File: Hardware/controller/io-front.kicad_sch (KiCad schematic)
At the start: 14 parts, among them J401 Conn_02x10_Odd_Even, J402 Conn_02x05_Odd_Even, J403 Conn_02x08_Odd_Even

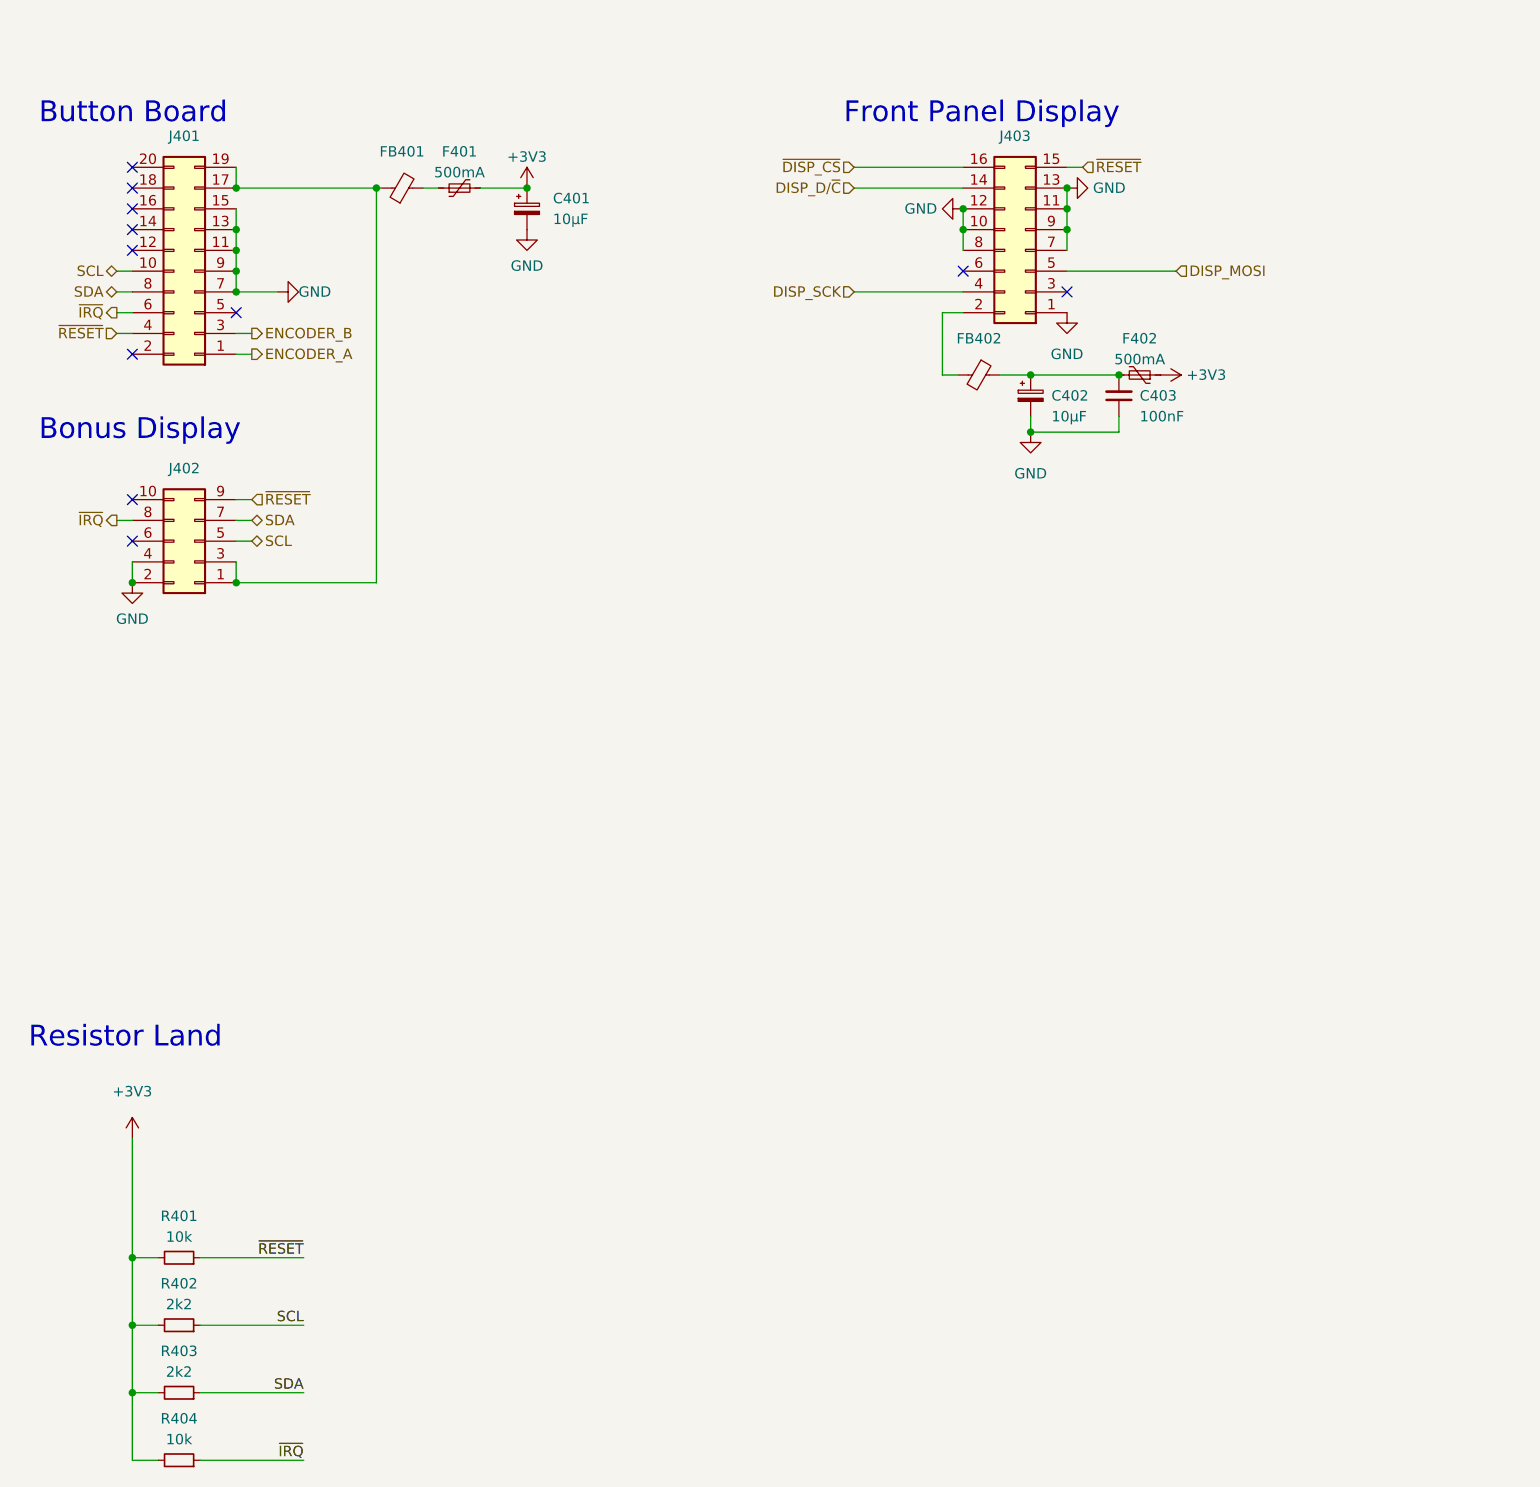
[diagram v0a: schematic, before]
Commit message: Begin cleaning up controller for rework
- Removed some of the old stuff

- Added USB host connector for front panel (including footprint for new
  ESD boi)
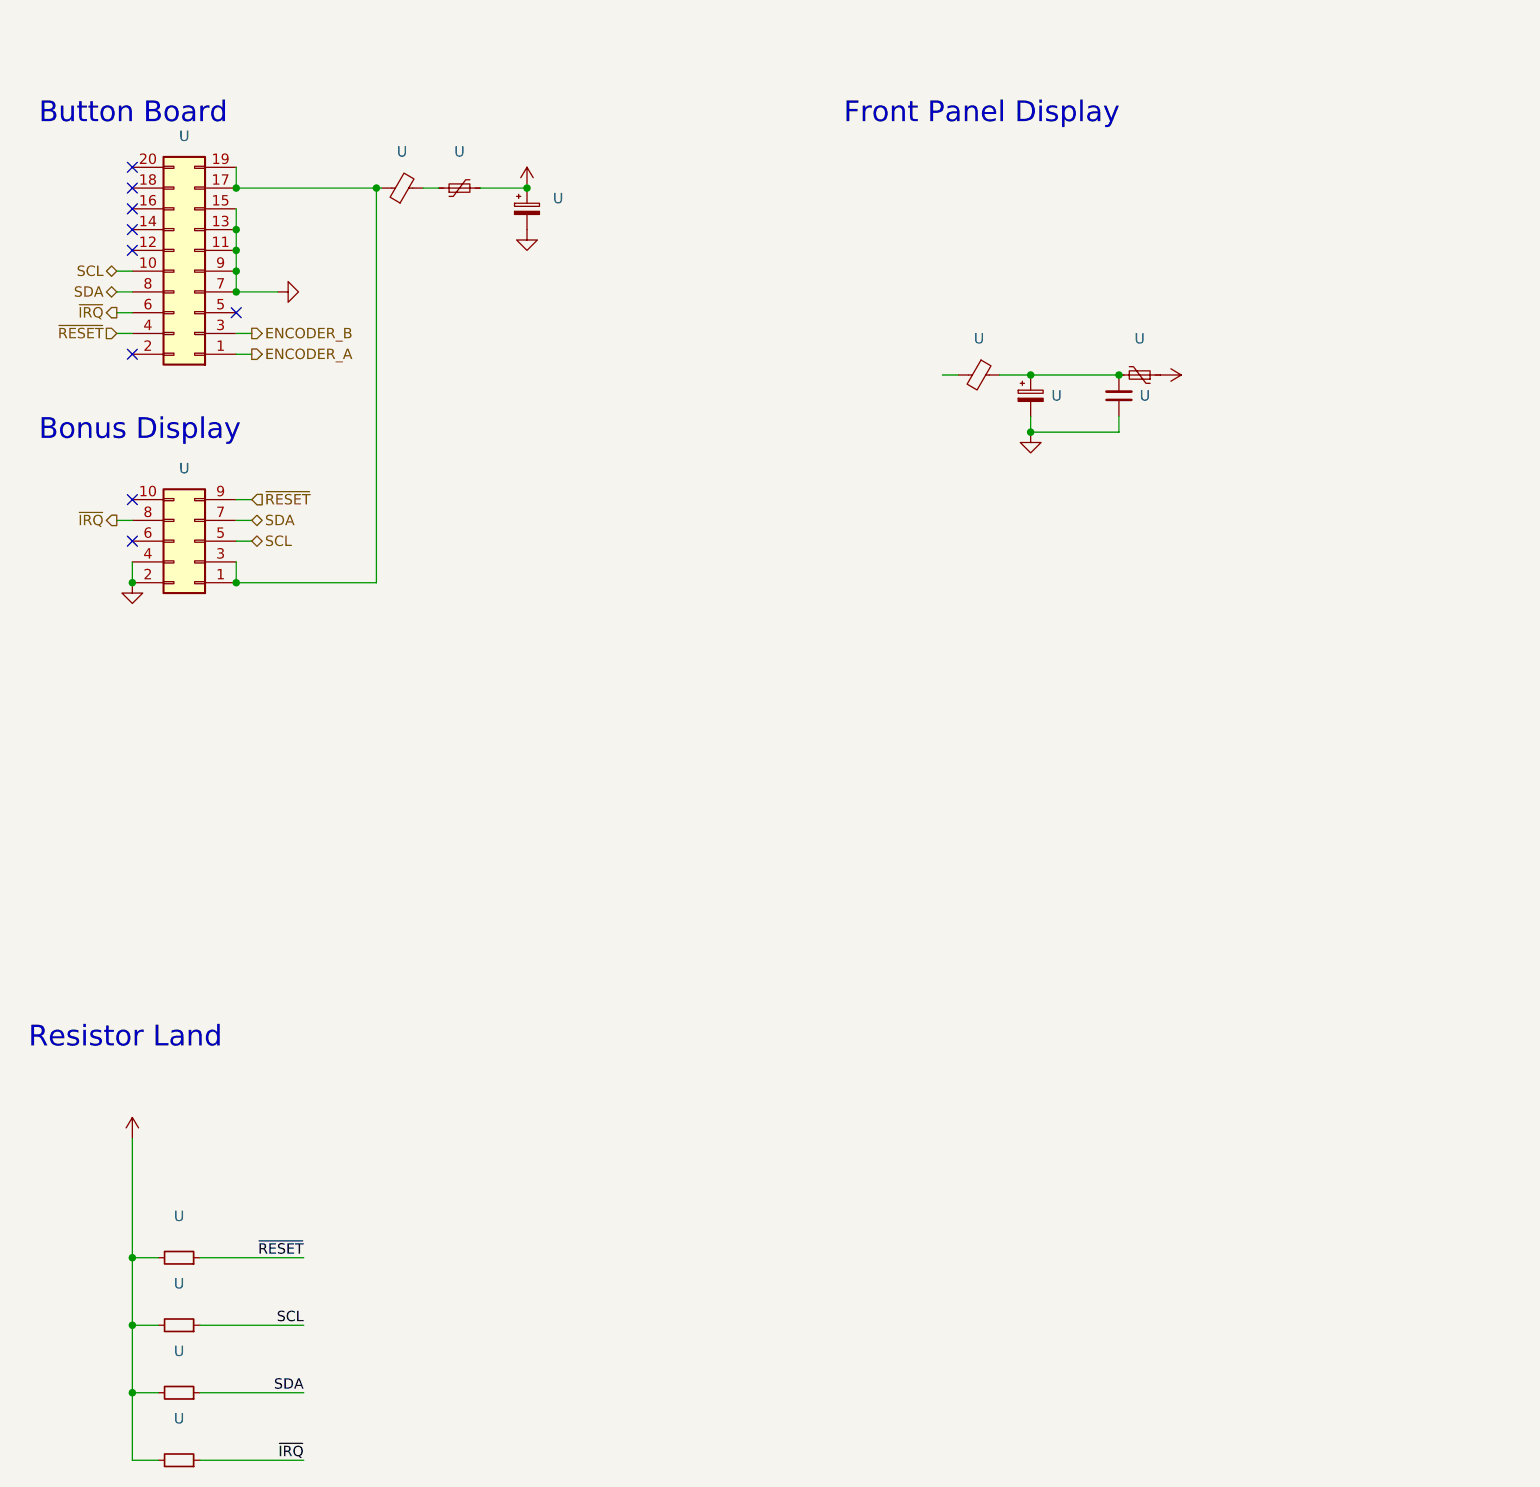
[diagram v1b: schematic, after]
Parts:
- removed J403: Conn_02x08_Odd_Even, Connector_IDC:IDC-Header_2x08_P2.54mm_Horizontal, symbol Connector_Generic:Conn_02x08_Odd_Even
- U: renamed from FB402; value FerriteBead_Small -> (none); footprint Inductor_SMD:L_0805_2012Metric_Pad1.05x1.20mm_HandSolder -> (none)
- U: renamed from J401; value Conn_02x10_Odd_Even -> (none); footprint Connector_PinHeader_1.27mm:PinHeader_2x10_P1.27mm_Vertical_SMD -> (none)
- U: renamed from C402; value 10µF -> (none); footprint Capacitor_Tantalum_SMD:CP_EIA-3216-18_Kemet-A_Pad1.58x1.35mm_HandSolder -> (none)
- U: renamed from C401; value 10µF -> (none); footprint Capacitor_Tantalum_SMD:CP_EIA-3216-18_Kemet-A_Pad1.58x1.35mm_HandSolder -> (none)
- U: renamed from R404; value 10k -> (none); footprint Resistor_SMD:R_0805_2012Metric_Pad1.20x1.40mm_HandSolder -> (none)
- U: renamed from R401; value 10k -> (none); footprint Resistor_SMD:R_0805_2012Metric_Pad1.20x1.40mm_HandSolder -> (none)
- U: renamed from R403; value 2k2 -> (none); footprint Resistor_SMD:R_0805_2012Metric_Pad1.20x1.40mm_HandSolder -> (none)
- U: renamed from R402; value 2k2 -> (none); footprint Resistor_SMD:R_0805_2012Metric_Pad1.20x1.40mm_HandSolder -> (none)
- U: renamed from J402; value Conn_02x05_Odd_Even -> (none); footprint Connector_PinHeader_1.27mm:PinHeader_2x05_P1.27mm_Vertical_SMD -> (none)
- U: renamed from F402; value 500mA -> (none); footprint Fuse:Fuse_1206_3216Metric_Pad1.42x1.75mm_HandSolder -> (none)
- U: renamed from F401; value 500mA -> (none); footprint Fuse:Fuse_1206_3216Metric_Pad1.42x1.75mm_HandSolder -> (none)
- U: renamed from C403; value 100nF -> (none); footprint Capacitor_SMD:C_0805_2012Metric_Pad1.18x1.45mm_HandSolder -> (none)
- U: renamed from FB401; value FerriteBead_Small -> (none); footprint Inductor_SMD:L_0805_2012Metric_Pad1.05x1.20mm_HandSolder -> (none)
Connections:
- no-connect marks 11 -> 9

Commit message: More work on controller; add MYIR SoM footprint
- Begin cleaning up the controller board, that is removing all of the
  old CPU stuff and replacing it with new stuff, and general cleanup

- Create a footprint for the STM32MP1 SoM (MYR MYC-YA151C family)
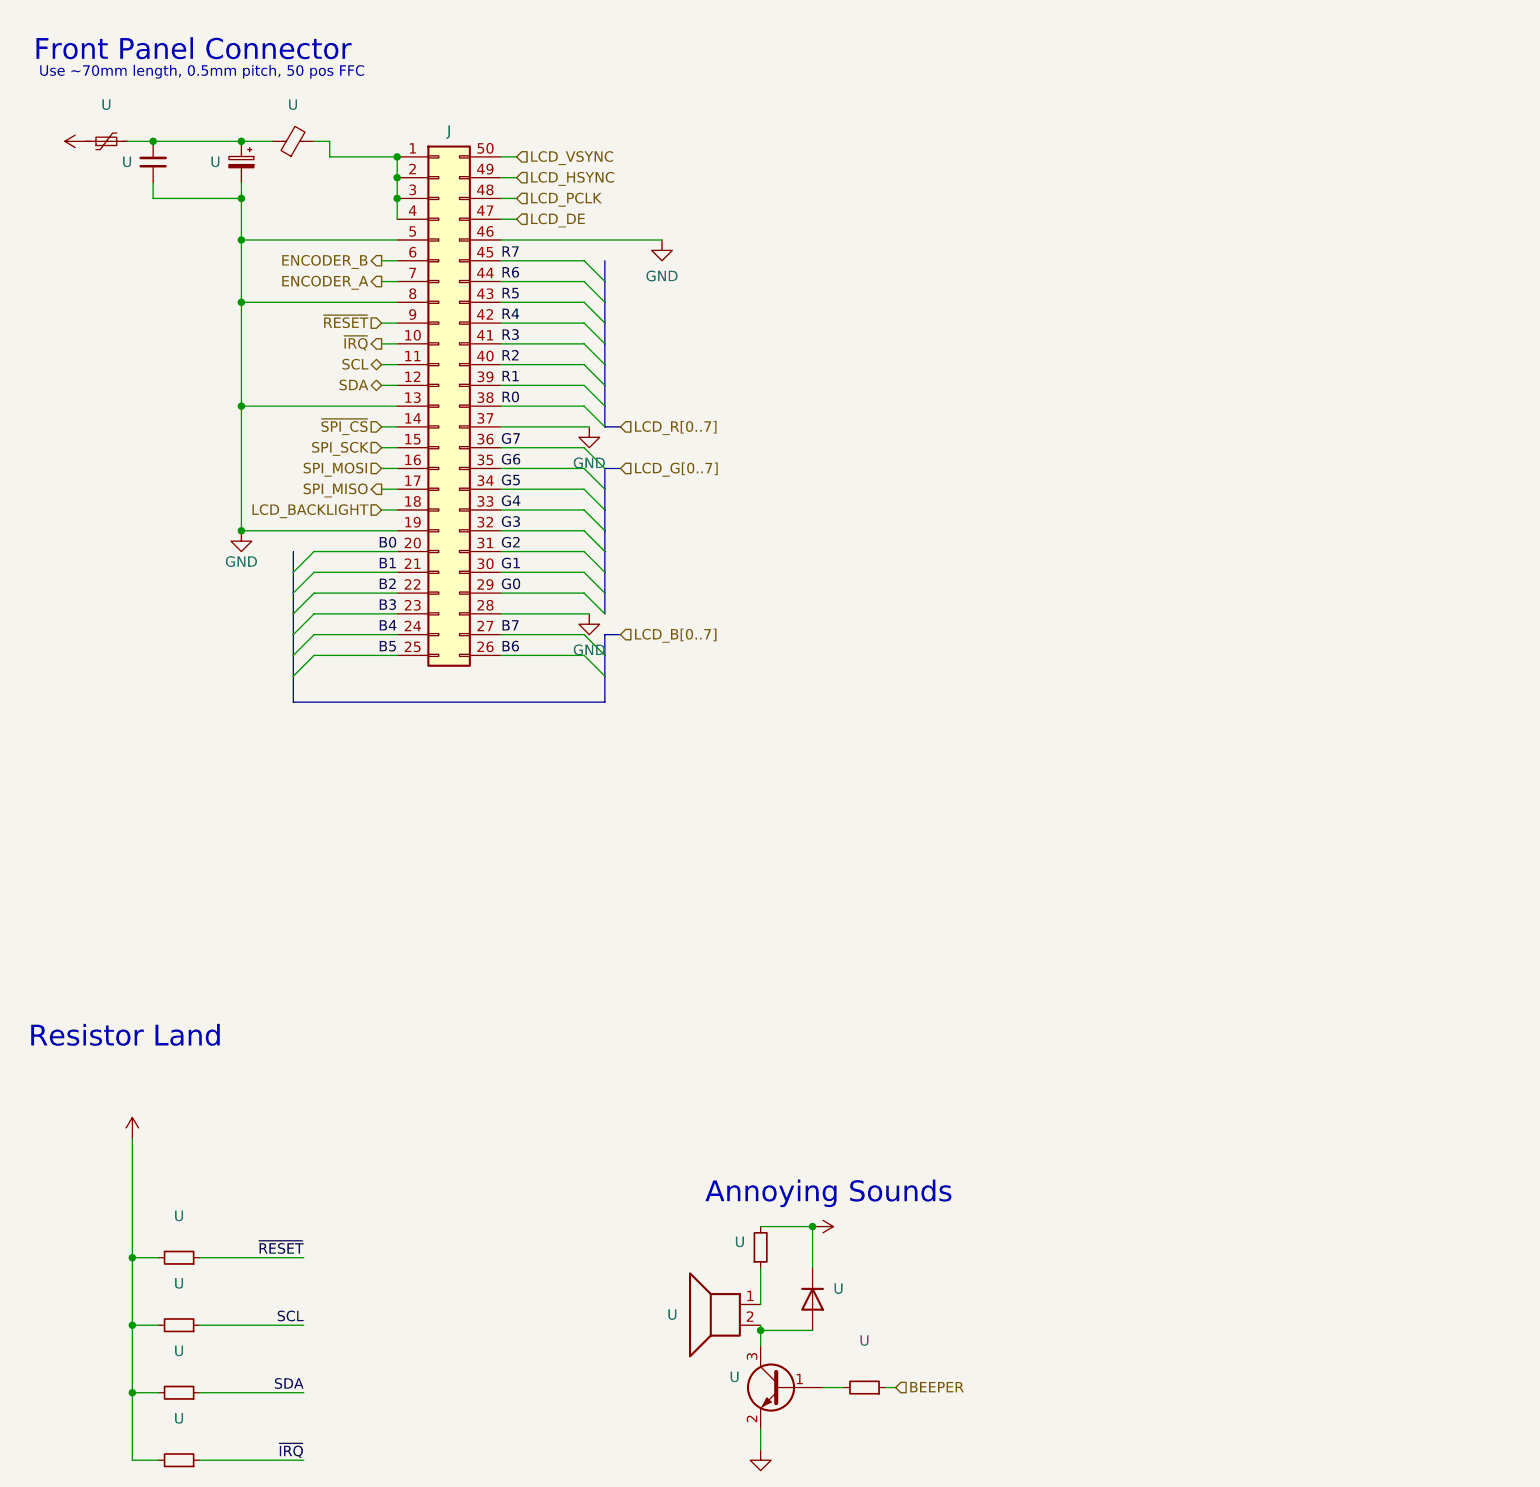
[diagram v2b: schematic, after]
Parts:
- removed U: (no value), symbol Device:FerriteBead_Small
- removed U: (no value), symbol Connector_Generic:Conn_02x10_Odd_Even
- removed U: (no value), symbol Device:C_Polarized_Small
- removed U: (no value), symbol Connector_Generic:Conn_02x05_Odd_Even
- removed U: (no value), symbol Device:Polyfuse_Small
- added J: Conn_02x25_Counter_Clockwise, symbol Connector_Generic:Conn_02x25_Counter_Clockwise
- added U (x2): (no value), symbol Device:R_Small
- added U: (no value), symbol Device:Speaker
- added U: (no value), symbol Diode:SM4007
- added U: (no value), symbol Transistor_BJT:MMBT3904
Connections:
- net +3V3: now also U.1, U.1 (K), U.2; no longer U.2
- net ENCODER_A: now also J.7 (Pin_7)
- net ENCODER_B: now also J.6 (Pin_6)
- net GND: now also J.13 (Pin_13), J.19 (Pin_19), J.28 (Pin_28), J.37 (Pin_37), J.46 (Pin_46), J.5 (Pin_5), J.8 (Pin_8), U.2 (E)
- net SCL: now also J.11 (Pin_11)
- net SDA: now also J.12 (Pin_12)
- net ~{IRQ}: now also J.10 (Pin_10)
- net ~{RESET}: now also J.9 (Pin_9)
- net at U.1, U.2: now also U.1, U.2
- net at U.2: now also J.1 (Pin_1), J.2 (Pin_2), J.3 (Pin_3), J.4 (Pin_4); no longer U.1
- new net: U.1, U.1
- new net: U.2, U.2 (A), U.3 (C)
- new net: U.1 (B), U.2
- new net B0: J.20 (Pin_20)
- new net B1: J.21 (Pin_21)
- new net B2: J.22 (Pin_22)
- new net B3: J.23 (Pin_23)
- new net B4: J.24 (Pin_24)
- new net B5: J.25 (Pin_25)
- new net B6: J.26 (Pin_26)
- new net B7: J.27 (Pin_27)
- new net BEEPER: U.1
- new net G0: J.29 (Pin_29)
- new net G1: J.30 (Pin_30)
- new net G2: J.31 (Pin_31)
- new net G3: J.32 (Pin_32)
- new net G4: J.33 (Pin_33)
- new net G5: J.34 (Pin_34)
- new net G6: J.35 (Pin_35)
- new net G7: J.36 (Pin_36)
- new net LCD_BACKLIGHT: J.18 (Pin_18)
- new net LCD_DE: J.47 (Pin_47)
- new net LCD_HSYNC: J.49 (Pin_49)
- new net LCD_PCLK: J.48 (Pin_48)
- new net LCD_VSYNC: J.50 (Pin_50)
- new net R0: J.38 (Pin_38)
- new net R1: J.39 (Pin_39)
- new net R2: J.40 (Pin_40)
- new net R3: J.41 (Pin_41)
- new net R4: J.42 (Pin_42)
- new net R5: J.43 (Pin_43)
- new net R6: J.44 (Pin_44)
- new net R7: J.45 (Pin_45)
- new net SPI_MISO: J.17 (Pin_17)
- new net SPI_MOSI: J.16 (Pin_16)
- new net SPI_SCK: J.15 (Pin_15)
- new net ~{SPI_CS}: J.14 (Pin_14)
- no-connect marks 9 -> 0
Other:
- note added: "Annoying Sounds"
- note added: "Front Panel Connector"
- note added: "Use ~70mm length, 0.5mm pitch, 50 pos FFC"
- note removed: "Bonus Display"
- note removed: "Button Board"
- note removed: "Front Panel Display"
- moved on the sheet: U
